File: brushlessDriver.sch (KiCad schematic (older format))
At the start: 28 parts

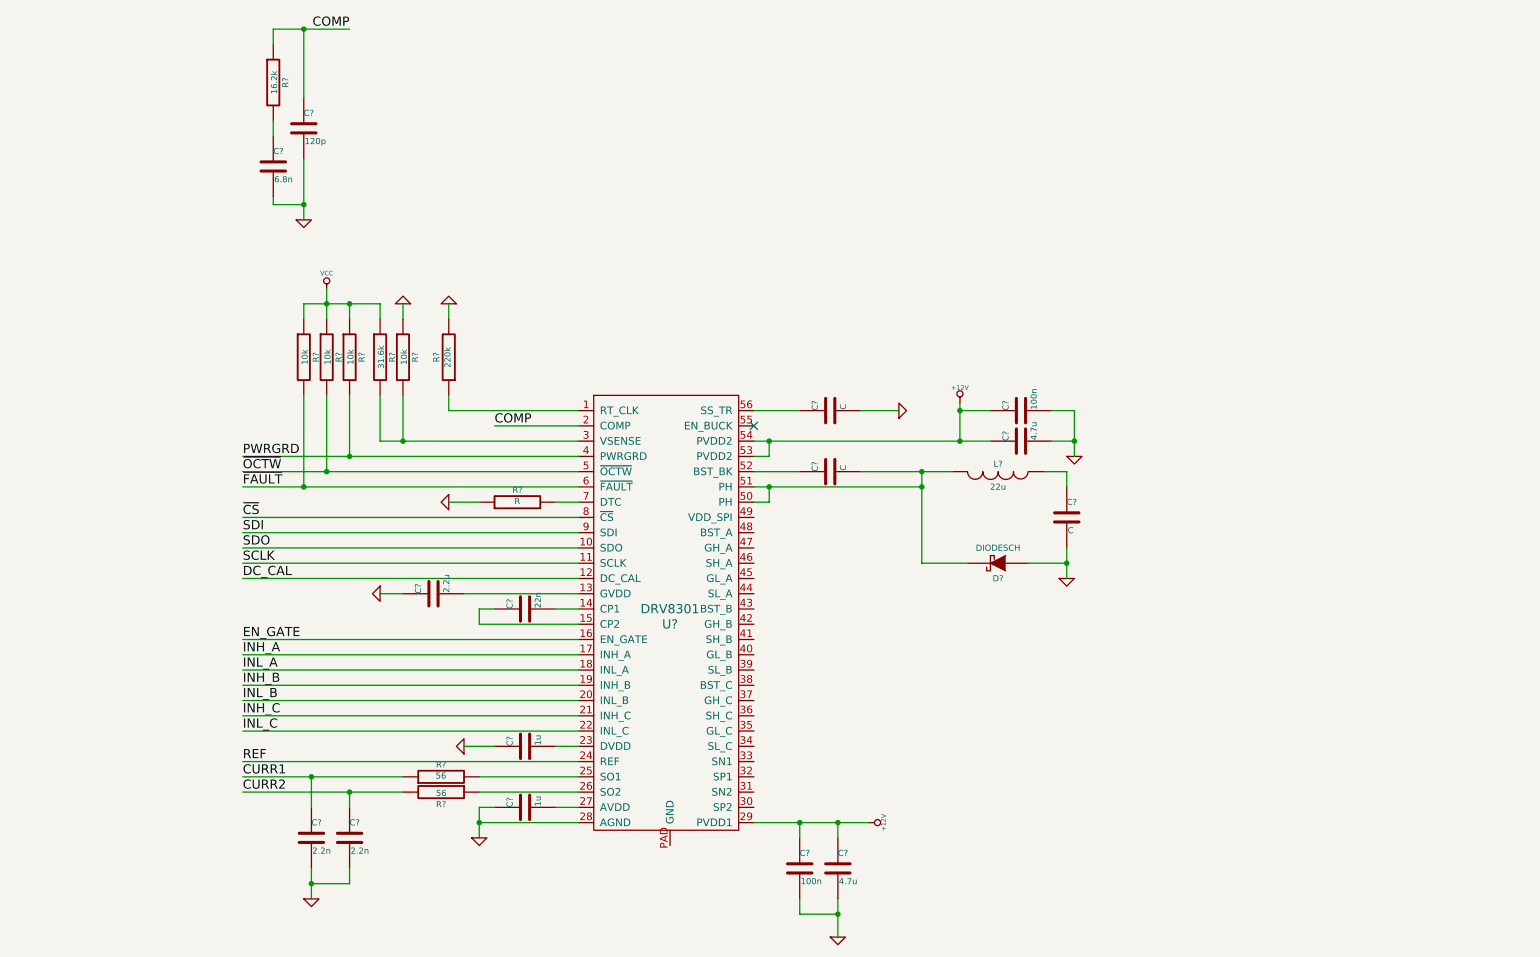
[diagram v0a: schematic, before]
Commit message: Finished routing. Needs some inspections about ground loops and supply rails.
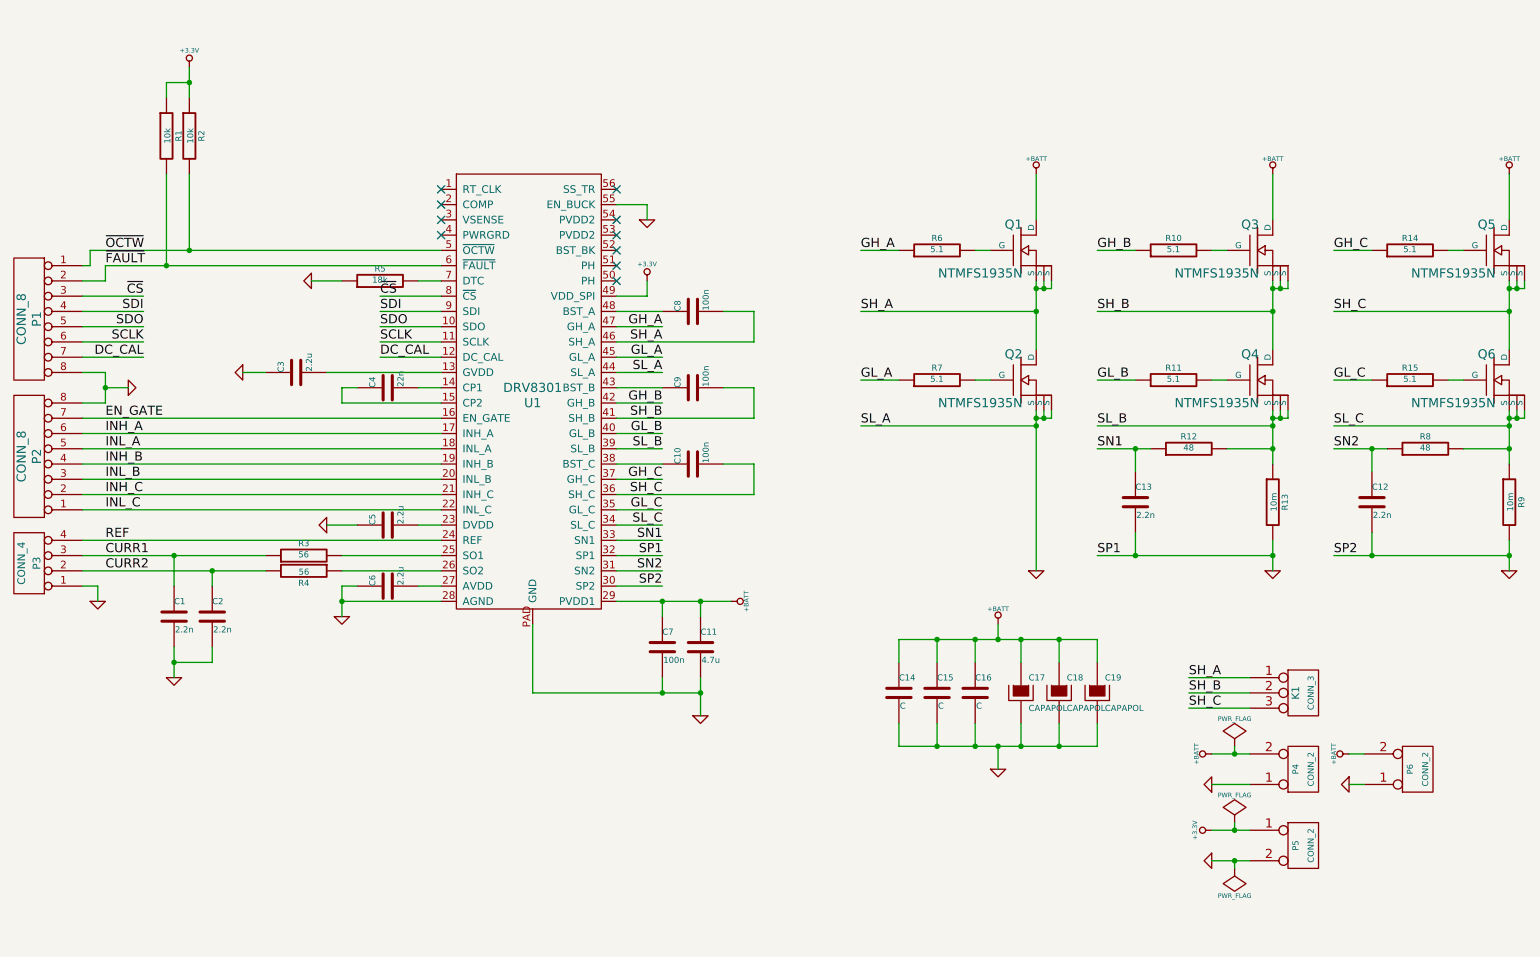
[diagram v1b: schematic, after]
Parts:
- removed C?: 120p, ~, symbol C
- removed C?: 6.8n, ~, symbol C
- removed C? (x3): C, ~, symbol C
- removed C?: 100n, ~, symbol C
- removed C?: 4.7u, ~, symbol C
- removed D?: DIODESCH, ~, symbol DIODESCH
- removed L?: 22u, ~, symbol INDUCTOR
- removed R? (x2): 10k, ~, symbol R
- removed R?: 16.2k, ~, symbol R
- removed R?: 31.6k, ~, symbol R
- removed R?: 220k, ~, symbol R
- added C10, C8, C9: 100n, ~, symbol C
- added C12, C13: 2.2n, ~, symbol C
- added C14, C15, C16: C, ~, symbol C
- added C17, C18, C19: CAPAPOL, ~, symbol CAPAPOL
- added K1: CONN_3, symbol CONN_3
- added P1, P2: CONN_8, symbol CONN_8
- added P3: CONN_4, symbol CONN_4
- added P4, P5, P6: CONN_2, symbol CONN_2
- added Q1, Q2, Q3, Q4, Q5, Q6: NTMFS1935N, ~, symbol NTMFS1935N
- added R10, R11, R14, R15, R6, R7: 5.1, ~, symbol R
- added R12, R8: 48, ~, symbol R
- added R13, R9: 10m, ~, symbol R
- C5, C6: renamed from C?; value 1u -> 2.2u
- R5: renamed from R?; value R -> 18k
- gave numbers to parts that had none: 11
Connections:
- net VCC is gone; now on net +3.3V: R1.1, R2.1
- net CURR1: now also P3.3 (P3)
- net CURR2: now also P3.2 (P2)
- net DC_CAL: now also P1.7 (P7)
- net EN_GATE: now also P2.7 (P7)
- net GND: now also U1.30 (SP2), U1.32 (SP1), U1.44 (SL_A), U1.55 (EN_BUCK), U1.PAD (GND), C12.2, C13.2, C14.2, C15.2, C16.2, C17.2, C18.2, C19.2, P1.8 (P8), P2.8 (P8), P3.1 (P1), P4.1 (P1), P5.2 (PM), P6.1 (P1), Q2.1 (S), Q2.2 (S), Q2.3 (S), R13.2, R9.2
- net INH_A: now also P2.6 (P6)
- net INH_B: now also P2.4 (P4)
- net INH_C: now also P2.2 (P2)
- net INL_A: now also P2.5 (P5)
- net INL_B: now also P2.3 (P3)
- net INL_C: now also P2.1 (P1)
- net REF: now also P3.4 (P4)
- net SCLK: now also P1.6 (P6)
- net SDI: now also P1.4 (P4)
- net SDO: now also P1.5 (P5)
- net ~CS: now also P1.3 (P3)
- net ~FAULT: now also P1.2 (P2)
- net ~OCTW: now also P1.1 (P1)
- net SN2: now reaches U1.31 (SN2)
- net SN2: now also C12.1, R8.1
- net SN1: now reaches U1.33 (SN1)
- net SN1: now also C13.1, R12.1
- net SL_C: now reaches U1.34 (SL_C)
- net SL_C: now also Q6.1 (S), Q6.2 (S), Q6.3 (S), R8.2, R9.1
- net GL_C: now reaches U1.35 (GL_C)
- net GL_C: now also R15.1
- net SH_C: now reaches U1.36 (SH_C)
- net SH_C: now also C10.2, K1.3 (P3), Q5.1 (S), Q5.2 (S), Q5.3 (S), Q6.5 (D)
- net GH_C: now reaches U1.37 (GH_C)
- net GH_C: now also R14.1
- net at U1.38 (BST_C): now also C10.1
- net SL_B: now reaches U1.39 (SL_B)
- net SL_B: now also Q4.1 (S), Q4.2 (S), Q4.3 (S), R12.2, R13.1
- net GL_B: now reaches U1.40 (GL_B)
- net GL_B: now also R11.1
- net SH_B: now reaches U1.41 (SH_B)
- net SH_B: now also C9.2, K1.2 (PM), Q3.1 (S), Q3.2 (S), Q3.3 (S), Q4.5 (D)
- net GH_B: now reaches U1.42 (GH_B)
- net GH_B: now also R10.1
- net at U1.43 (BST_B): now also C9.1
- net GL_A: now reaches U1.45 (GL_A)
- net GL_A: now also R7.1
- net SH_A: now reaches U1.46 (SH_A)
- net SH_A: now also C8.2, K1.1 (P1), Q1.1 (S), Q1.2 (S), Q1.3 (S), Q2.5 (D)
- net GH_A: now reaches U1.47 (GH_A)
- net GH_A: now also R6.1
- net at U1.48 (BST_A): now also C8.1
- net +3.3V: now reaches U1.49 (VDD_SPI)
- net +3.3V: now also P5.1 (P1)
- net at U1.50 (PH): no longer U1.51 (PH)
- net +12V renamed +BATT
- net +BATT: now also C14.1, C15.1, C16.1, C17.1, C18.1, C19.1, P4.2 (PM), P6.2 (PM), Q1.5 (D), Q3.5 (D), Q5.5 (D); no longer U1.53 (PVDD2), U1.54 (PVDD2)
- net COMP: no longer names the net of U1.2 (COMP)
- net PWRGRD: no longer names the net of U1.4 (PWRGRD)
- new net: Q1.4 (G), R6.2
- new net: Q2.4 (G), R7.2
- new net: Q3.4 (G), R10.2
- new net: Q4.4 (G), R11.2
- new net: Q5.4 (G), R14.2
- new net: Q6.4 (G), R15.2
- no-connect marks 1 -> 10
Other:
- moved on the sheet: C1, C11, C2, C3, C4, C5, C6, C7, R1, R2, R3, R4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
